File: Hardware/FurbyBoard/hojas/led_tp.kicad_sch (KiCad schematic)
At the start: 10 parts, among them J11 J_EXP: header de expansión si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

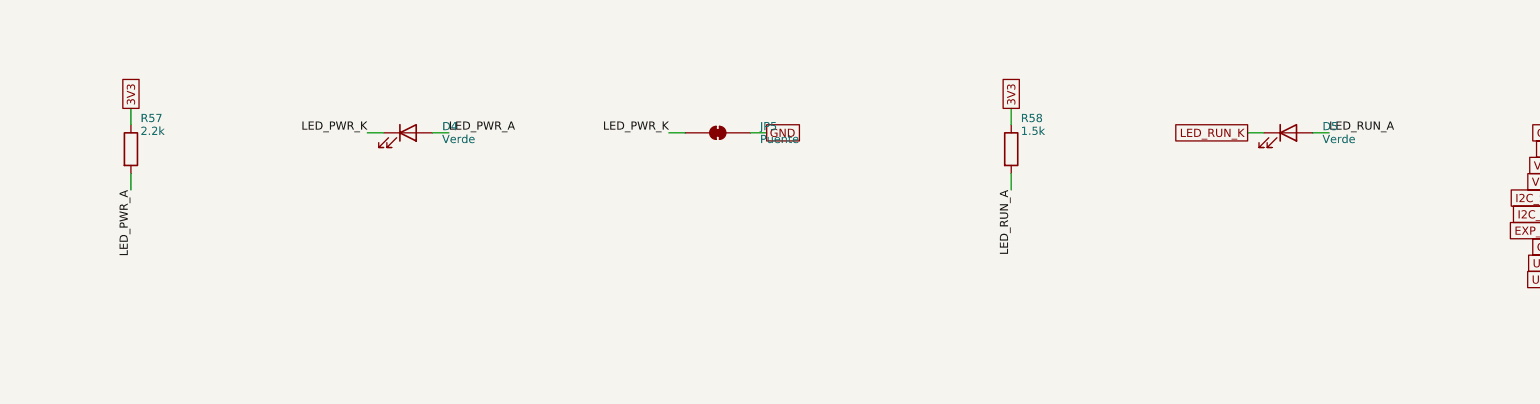
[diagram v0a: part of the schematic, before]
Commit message: Refactor: pads de cable agrupados por zona y etiquetas globales
- Motor en J9 con leva, encoder y sensores; altavoz en J8 con inclinación y
  lengua; luz en J7 con el IR. Desaparecen J4 y J10: cada grupo sale por el
  borde más cercano a su destino.
- Micro en 2x03 en vez de 1x06 para que quepa junto al borde derecho.
- Todas las etiquetas del esquemático son globales, así el nombre de red
  coincide con el del PCB (paridad sin prefijos de hoja).
- ERC 0 errores, 0 avisos.

Co-Authored-By: Claude Opus 5.5 (1M context) <noreply@anthropic.com>
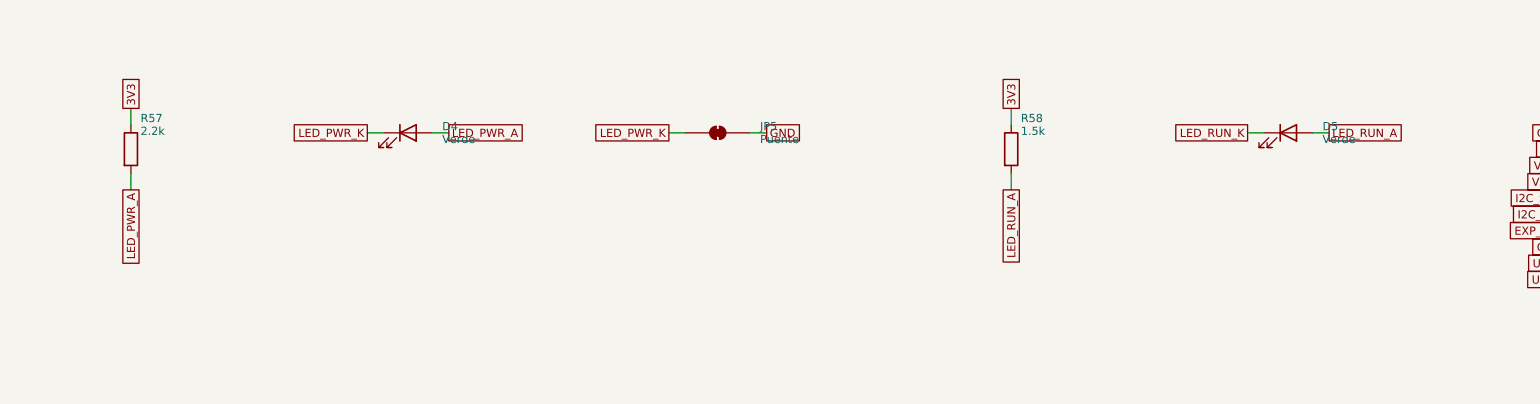
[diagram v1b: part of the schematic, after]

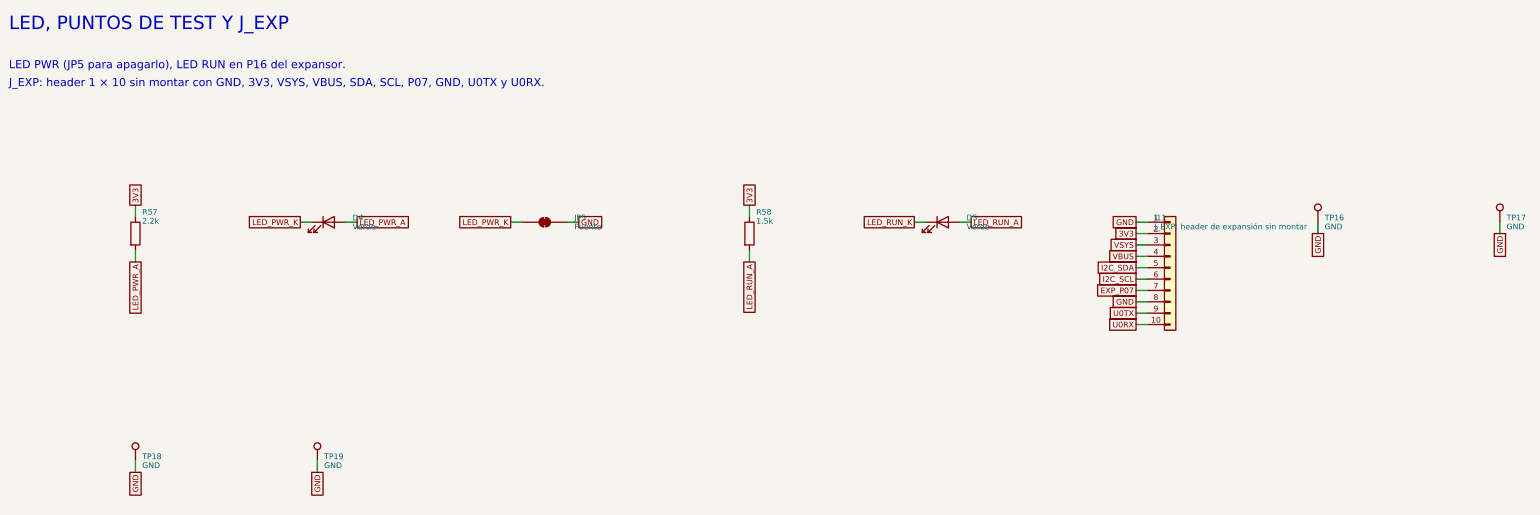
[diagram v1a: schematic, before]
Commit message: Feature: par USB trazado, planos GND/VSYS y serigrafía de la FurbyBoard
- Par USB de J1 al ESD y al módulo, acoplado 0,28/0,15 por F.Cu sobre el
  plano de GND, sin vías (rutas_fijas.py, bloqueado para el autorrutado).
  Canal libre en x -83 bajo la batería.
- In1 plano de GND e In2 plano de VSYS; potencia por pista a 0,4 (cabe en
  los pads de 0,5 de paso) y 3V3 a 0,3. exportar_dsn.py deja el DSN para
  Freerouting con las clases de red.
- Rótulos de serigrafía colocados solos (serigrafia.py): TP, LED, botones,
  puentes y polaridad de la batería arriba; función de cada pad de cable y
  GPIO del J_EXP abajo, con leyenda para J7, J9 y J5.
- Para que quepan los rótulos: fila de LED con resistencias debajo, botones
  en vertical, rejilla de TP con el rótulo debajo. Quedan 14 TP: fuera EN e
  IO0 (se miden en los pads de SW1 y SW2), CHG y PG (en D1 y D2) y un GND.

ERC 0/0. DRC 0 salvo una vía de GND sin plano relleno; sin rutar.

Co-Authored-By: Claude Opus 5.5 (1M context) <noreply@anthropic.com>
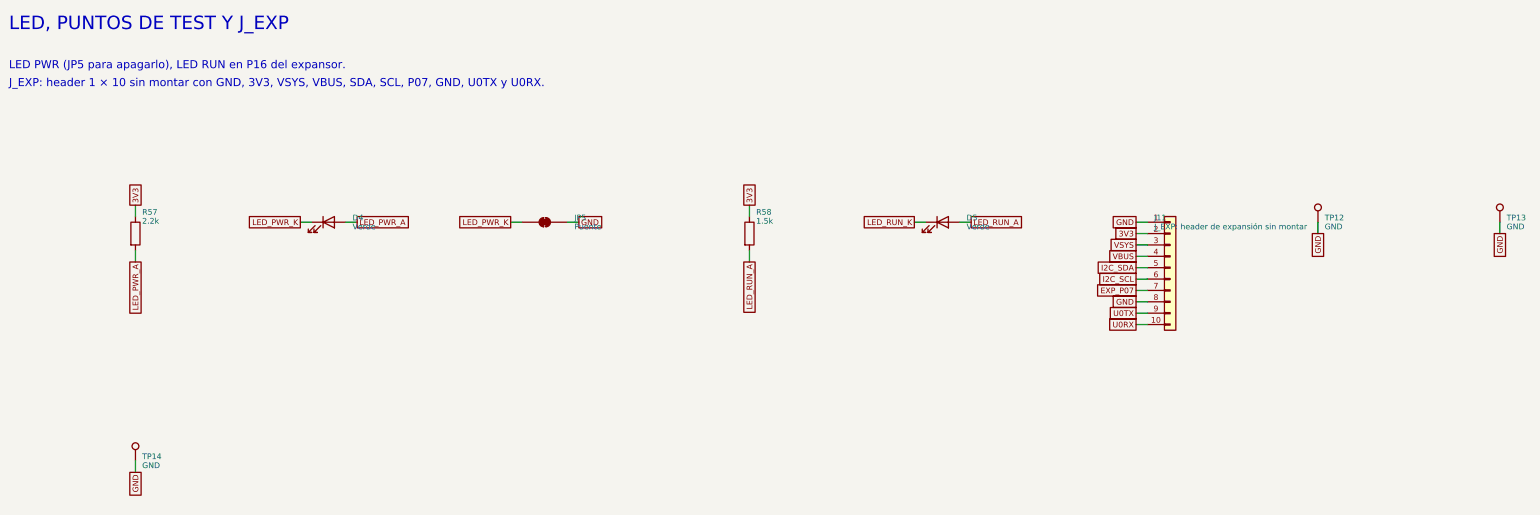
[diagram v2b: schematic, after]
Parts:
- removed TP16, TP17, TP18, TP19: GND, TestPoint:TestPoint_Pad_D1.5mm, symbol Connector:TestPoint
- added TP12, TP13, TP14: GND, TestPoint:TestPoint_Pad_D1.5mm, symbol Connector:TestPoint
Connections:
- net GND: now also TP12.1, TP13.1, TP14.1

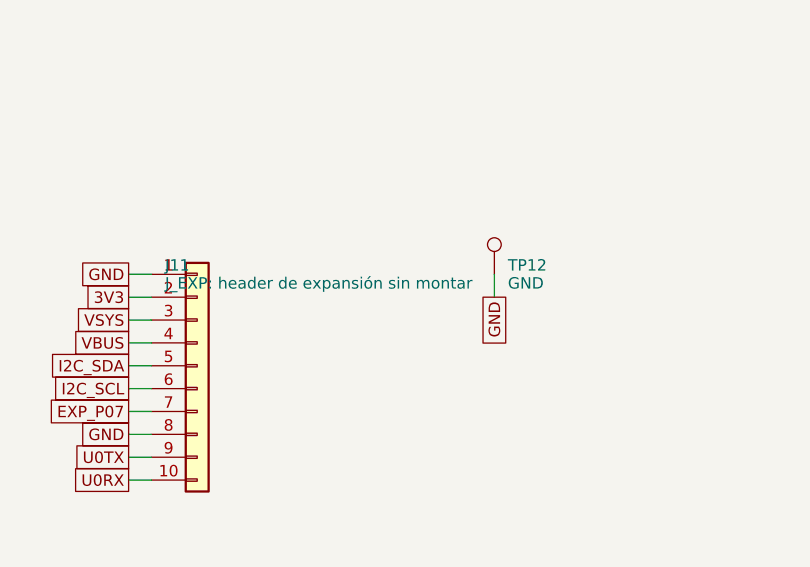
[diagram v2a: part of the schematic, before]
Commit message: Feature: esquema de la FurbyBoard al procedimiento nuevo: rúbrica L, reglas por red, pines por geometría y simulación del elevador
- Rúbrica S/M/L (L) y tabla de raíles con anchos mínimos (params.ANCHOS_MINIMOS), que gen_pro.py vuelca al .kicad_dru como una regla por red, con cuellos dentro de los patios de los QFN y de J1.
- Vías de 0,45/0,2 solo en la clase USB (cruce del par en el receptáculo de 16 pines); el resto sigue en 0,6/0,3.
- pcb-toolkit.toml: clases B/C/D, anchos, grupos explícitos y zonas del puente H y de la clase D.
- Redes a la convención: BB_SW1/2, I2S_SCK_MIC/I2S_WS_MIC.
- Pines del módulo (I2S, HOME, EXP_INT) y puertos del TCA9535 por geometría, sin tocar strapping, USB ni ADC.
- LED del encoder desde V6 por 470 ohm (sin Q2); J_EXP 2x5; J9 y J5 reordenados; serigrafía al día.
- ERC 0/0. Simulación ngspice del elevador en el peor caso (sim/). Informes de las puertas A y B en revisiones/; un crítico (NTC del cargador) queda escalado.

Co-Authored-By: Claude Fable 5.1 <noreply@anthropic.com>
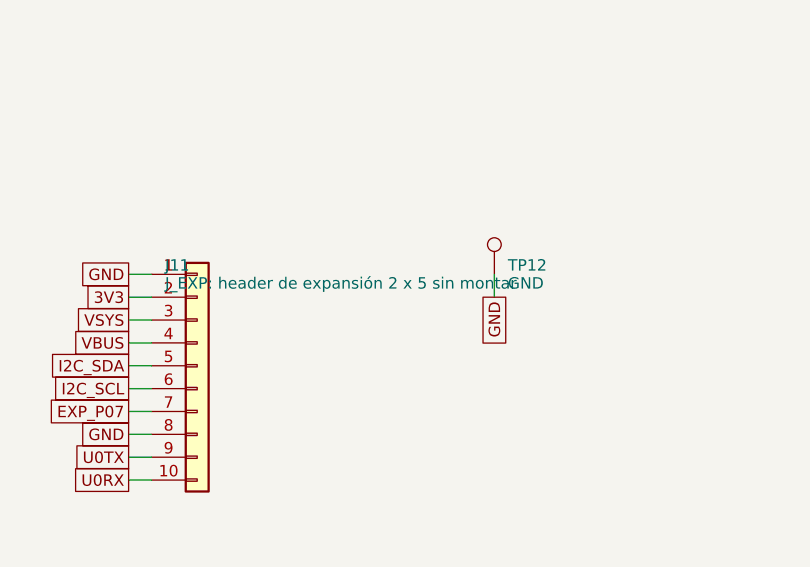
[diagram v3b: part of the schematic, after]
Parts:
- J11: value J_EXP: header de expansión sin montar -> J_EXP: header de expansión 2 x 5 sin montar; footprint FurbyBoard:Pads_1x10_P2.54mm -> FurbyBoard:Pads_2x05_P2.54mm
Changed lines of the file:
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@@
 			)
 		)
-		(property "Value" "J_EXP: header de expansión sin montar"
+		(property "Value" "J_EXP: header de expansión 2 x 5 sin montar"
 			(at 275.82 67.04 0)
 			(show_name no)
@@
 			)
 		)
-		(property "Footprint" "FurbyBoard:Pads_1x10_P2.54mm"
+		(property "Footprint" "FurbyBoard:Pads_2x05_P2.54mm"
 			(at 279.4 76.2 0)
 			(hide yes)
@@
 			)
 		)
-		(property "Description" "J_EXP: header de expansión sin montar"
+		(property "Description" "J_EXP: header de expansión 2 x 5 sin montar"
 			(at 279.4 76.2 0)
 			(hide yes)

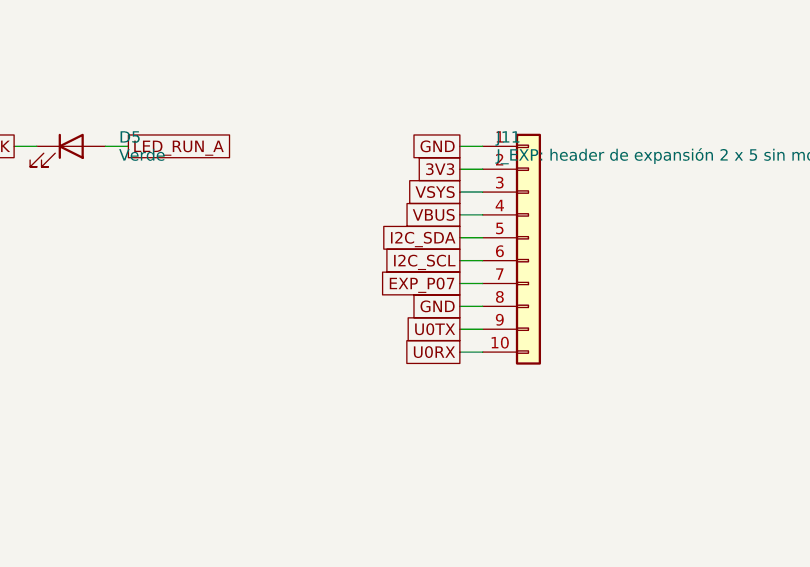
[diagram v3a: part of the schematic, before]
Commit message: Feature: UART0 del módulo a J11 por In3 (bloque U)
J11 permutado (5 EXP_P07, 6 SCL, 7 U0TX, 9 SDA, 10 U0RX; alimentaciones
sin cambios). TX y RX salen por In3 bajo el keepout de la antena, cruzan
J7 por la fila entre sus dos hileras y por la franja al sur, bajan en
pareja por el oeste de H1 y el este de J8/J5 y entran en J11.7 y J11.10.
SDA cruza a J8 por F.Cu (en In3 cerraba el paso; en In2 aislaba VSYS) y
EXP_P07 baja por In3 entre las vías del clase D y del I2S hasta J11.5.

Puerta D: ERC 0, DRC 0 con paridad 0 (1 sin unir: IR_PWR), revisar-rutado
0 errores, rellenos VSYS In2 en 3 trozos (2613 mm2) y GND sin trozos nuevos.
PNG revisados: In3 de J7/H1, de J5/J11 y de la salida del módulo; F del
cruce de SDA y de la vía de RX.

Co-Authored-By: Claude Opus 5.5 (1M context) <noreply@anthropic.com>
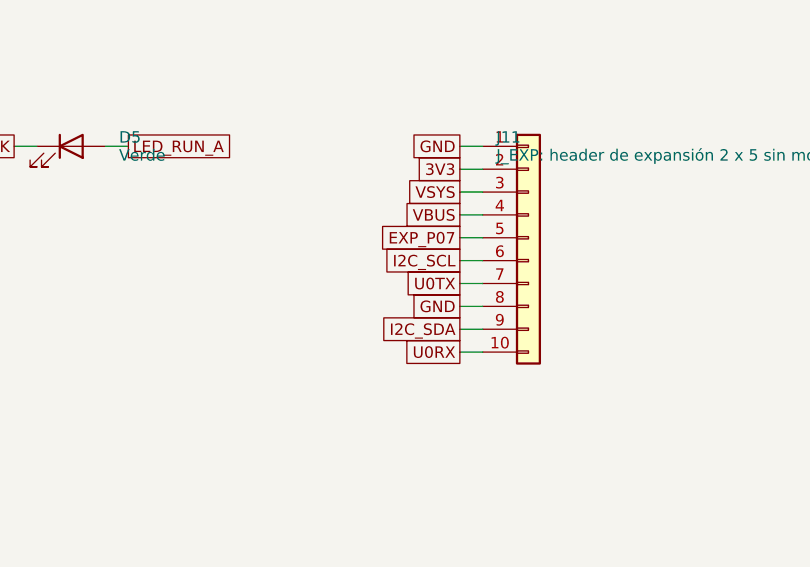
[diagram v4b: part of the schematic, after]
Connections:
- net EXP_P07: now also J11.5 (Pin_5); no longer J11.7 (Pin_7)
- net I2C_SDA: now also J11.9 (Pin_9); no longer J11.5 (Pin_5)
- net U0TX: now also J11.7 (Pin_7); no longer J11.9 (Pin_9)
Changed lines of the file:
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@@
 		)
 	)
-	(global_label "I2C_SDA"
+	(global_label "EXP_P07"
 		(shape passive)
 		(at 271.78 76.2 180)
@@
 		)
 	)
-	(global_label "EXP_P07"
+	(global_label "U0TX"
 		(shape passive)
 		(at 271.78 81.28 180)
@@
 		)
 	)
-	(global_label "U0TX"
+	(global_label "I2C_SDA"
 		(shape passive)
 		(at 271.78 86.36 180)

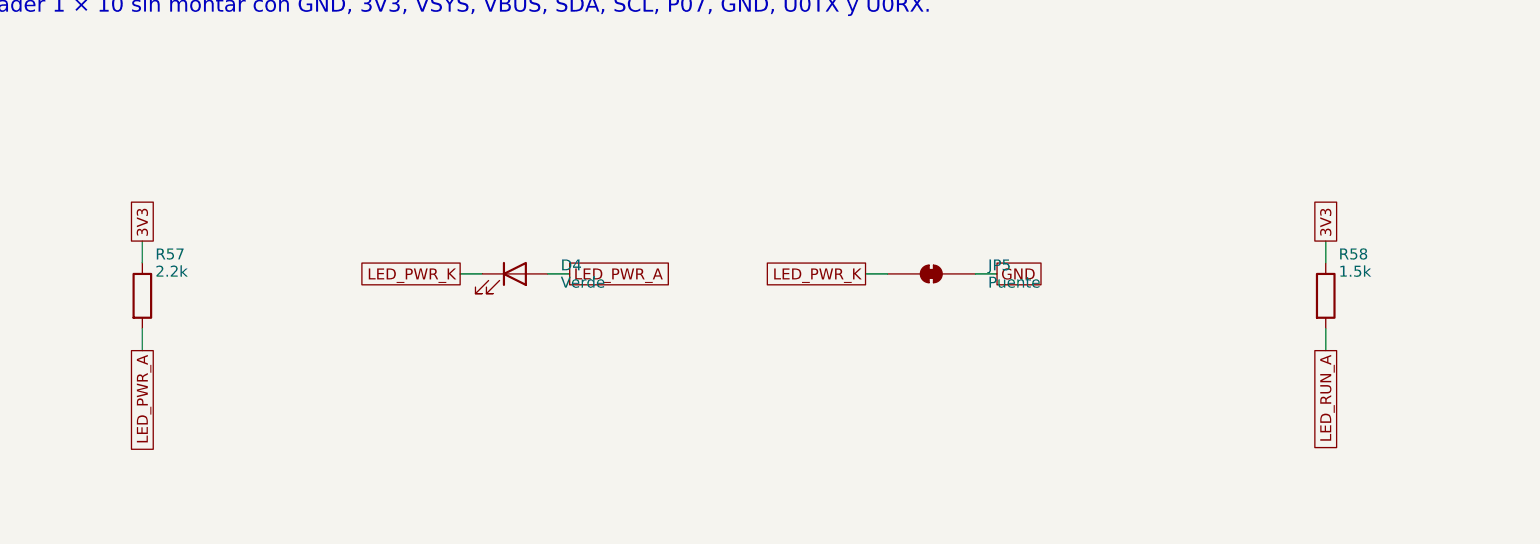
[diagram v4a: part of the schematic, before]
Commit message: Fix: C41 de 10 µF junto a VDD de U7 y R57/R58 a 1 kΩ (arreglos de la simulación)
- C41 (C19702, 10 µF 10 V X5R 0603) al oeste de C26, a 1,3 mm de los pines 7/8,
  del lado de los pines del puente de VSYS de B.Cu; VSYS al tronco de los pines
  (0,6 mm, y -86,075) y GND por su vía al oeste. sim: 257 mV pp en VDD con solo C26.
- Micromovimientos: vía de TONGUE_PAD 0,7 mm al norte (diagonal desde R44.2; B.Cu por
  y -83,55) y segunda vía de VSYS del puente de x -97,0 a -96,875 (baja en F.Cu al
  tramo de C41). Ni I2S ni salidas al altavoz tocados.
- R57 y R58 de 2,2 kΩ / 1,5 kΩ a 1 kΩ (C21190): D4/D5 son verdes InGaN (2,6–3,1 V).

Puertas: ERC 0; DRC con paridad 0 infracciones, 0 sin unir; revisar-rutado PASS
(0 errores, los mismos 152 avisos que antes); rellenos sin islas nuevas (GND In1/In4
3279,4 mm² en 1, F 2055,0 en 21, B 2758,1 en 11; VSYS In2 2583,6 en 3).
PNG revisados: F.Cu, B.Cu, In2 y cobre de la ventana de U7/C41/R44 (10 × 10 mm).

Co-Authored-By: Claude Opus 5.5 (1M context) <noreply@anthropic.com>
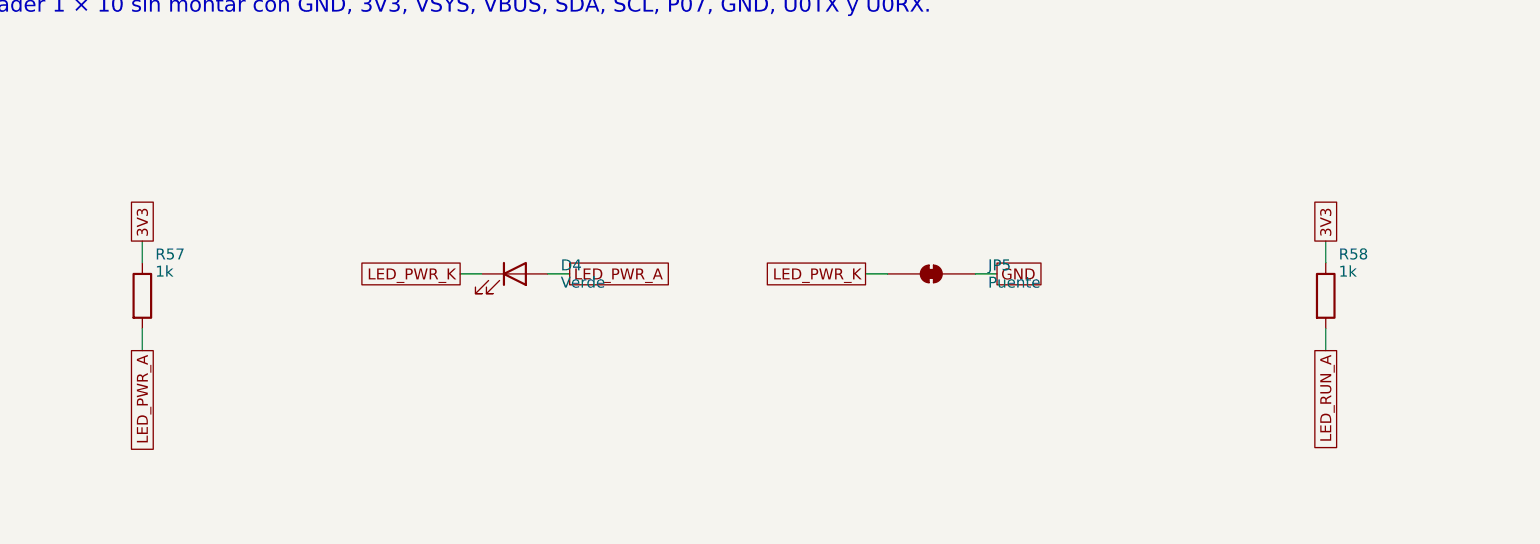
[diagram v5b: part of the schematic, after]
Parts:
- R57: value 2.2k -> 1k; LCSC C4190 -> C21190
- R58: value 1.5k -> 1k; LCSC C22843 -> C21190
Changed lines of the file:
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@@
 			)
 		)
-		(property "Value" "1.5k"
+		(property "Value" "1k"
 			(at 186.92 65.77 0)
 			(show_name no)
@@
 			)
 		)
-		(property "Description" "LED RUN ≈ 0,9 mA"
-			(at 185.42 68.58 0)
-			(hide yes)
-			(show_name no)
-			(do_not_autoplace no)
-			(effects
-				(font
-					(size 1.27 1.27)
-				)
-				(justify left)
-			)
-		)
-		(property "LCSC" "C22843"
+		(property "Description" "LED RUN ≈ 0,4–0,75 mA (verde InGaN, VF 2,6–3,1 V)"
+			(at 185.42 68.58 0)
+			(hide yes)
+			(show_name no)
+			(do_not_autoplace no)
+			(effects
+				(font
+					(size 1.27 1.27)
+				)
+				(justify left)
+			)
+		)
+		(property "LCSC" "C21190"
 			(at 185.42 68.58 0)
 			(hide yes)
@@
 			)
 		)
-		(property "Value" "2.2k"
+		(property "Value" "1k"
 			(at 49.76 65.77 0)
 			(show_name no)
@@
 			)
 		)
-		(property "Description" "LED PWR ≈ 0,6 mA"
-			(at 48.26 68.58 0)
-			(hide yes)
-			(show_name no)
-			(do_not_autoplace no)
-			(effects
-				(font
-					(size 1.27 1.27)
-				)
-				(justify left)
-			)
-		)
-		(property "LCSC" "C4190"
+		(property "Description" "LED PWR ≈ 0,4–0,75 mA (verde InGaN, VF 2,6–3,1 V)"
+			(at 48.26 68.58 0)
+			(hide yes)
+			(show_name no)
+			(do_not_autoplace no)
+			(effects
+				(font
+					(size 1.27 1.27)
+				)
+				(justify left)
+			)
+		)
+		(property "LCSC" "C21190"
 			(at 48.26 68.58 0)
 			(hide yes)
@@
 			)
 		)
-		(property "Description" "Cortar para apagar el LED PWR (−0,6 mA en reposo)"
+		(property "Description" "Cortar para apagar el LED PWR (hasta −0,75 mA en reposo)"
 			(at 139.7 66.04 0)
 			(hide yes)
